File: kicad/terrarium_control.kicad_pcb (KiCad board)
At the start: 2 copper layers, 48 parts, among them J1 5V_IN, J10 220V_OUT, J11 LAMP0, J12 LAMP1, J13 I2C, J2 5V_OUT, J3 12V_IN, J4 SWITCHERS, J5 ICSP, J6 FUN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

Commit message: ~50% of board layout completed
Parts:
- added JP1: 0R, Resistor_SMD:R_1206_3216Metric_Pad1.30x1.75mm_HandSolder, F.Cu at (134.1, 64.1)
- BT1: footprint Battery:BatteryHolder_Keystone_106_1x20mm -> terrarium_control:batt_holder
- moved C3 158.4 mm to (125.9, 59.4), turned to 90 degrees
- moved C7 158.3 mm to (138.5, 59.9), turned to 180 degrees
- moved R5 125.8 mm to (149.1, 68.0), turned to 270 degrees
- moved BT1 123.4 mm to (146.4, 58.4)
- moved R10 122.0 mm to (137.8, 75.4), turned to 180 degrees
- moved R13 121.6 mm to (141.2, 75.4)
- moved U2 121.5 mm to (138.0, 79.9), turned to 270 degrees
- moved R9 120.6 mm to (121.3, 77.2), turned to 180 degrees
- moved C4 117.5 mm to (123.3, 59.8), turned to 90 degrees
- moved RN1 115.2 mm to (129.5, 74.5), turned to 270 degrees
- moved J3 97.8 mm to (142.0, 80.9), turned to 180 degrees
- moved R8 95.2 mm to (125.7, 77.2), turned to 180 degrees
- moved J13 91.3 mm to (138.0, 72.4), turned to 90 degrees
- moved J5 89.9 mm to (115.2, 67.7), turned to 180 degrees
- moved R6 89.0 mm to (133.3, 77.2), turned to 180 degrees
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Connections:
- net Net-(U3-Pad1) renamed /X+
- net Net-(U3-Pad2) renamed /X-
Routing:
- net SQW: track 0.00 -> 20.6 mm
- net +5V: track 14.4 -> 32.9 mm
- net SCL: track 6.27 -> 21.3 mm
- net GND: track 0.00 -> 14.8 mm
- net MCU_RXD: track 0.00 -> 13.3 mm
- net SDA: track 3.56 -> 15.7 mm
- net +BATT: track 0.00 -> 11.2 mm
- net MCU_TXD: track 0.00 -> 10.3 mm
- net DAC: track 0.00 -> 9.05 mm
- net Net-(R8-Pad2): track 0.00 -> 6.26 mm
- net DAC3: track 0.00 -> 5.57 mm
- net Net-(Q2-Pad1): track 0.00 -> 4.93 mm
- net FUN: track 0.00 -> 4.61 mm
- net Net-(R6-Pad2): track 0.00 -> 3.88 mm
- net Net-(R7-Pad2): track 0.00 -> 3.88 mm
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
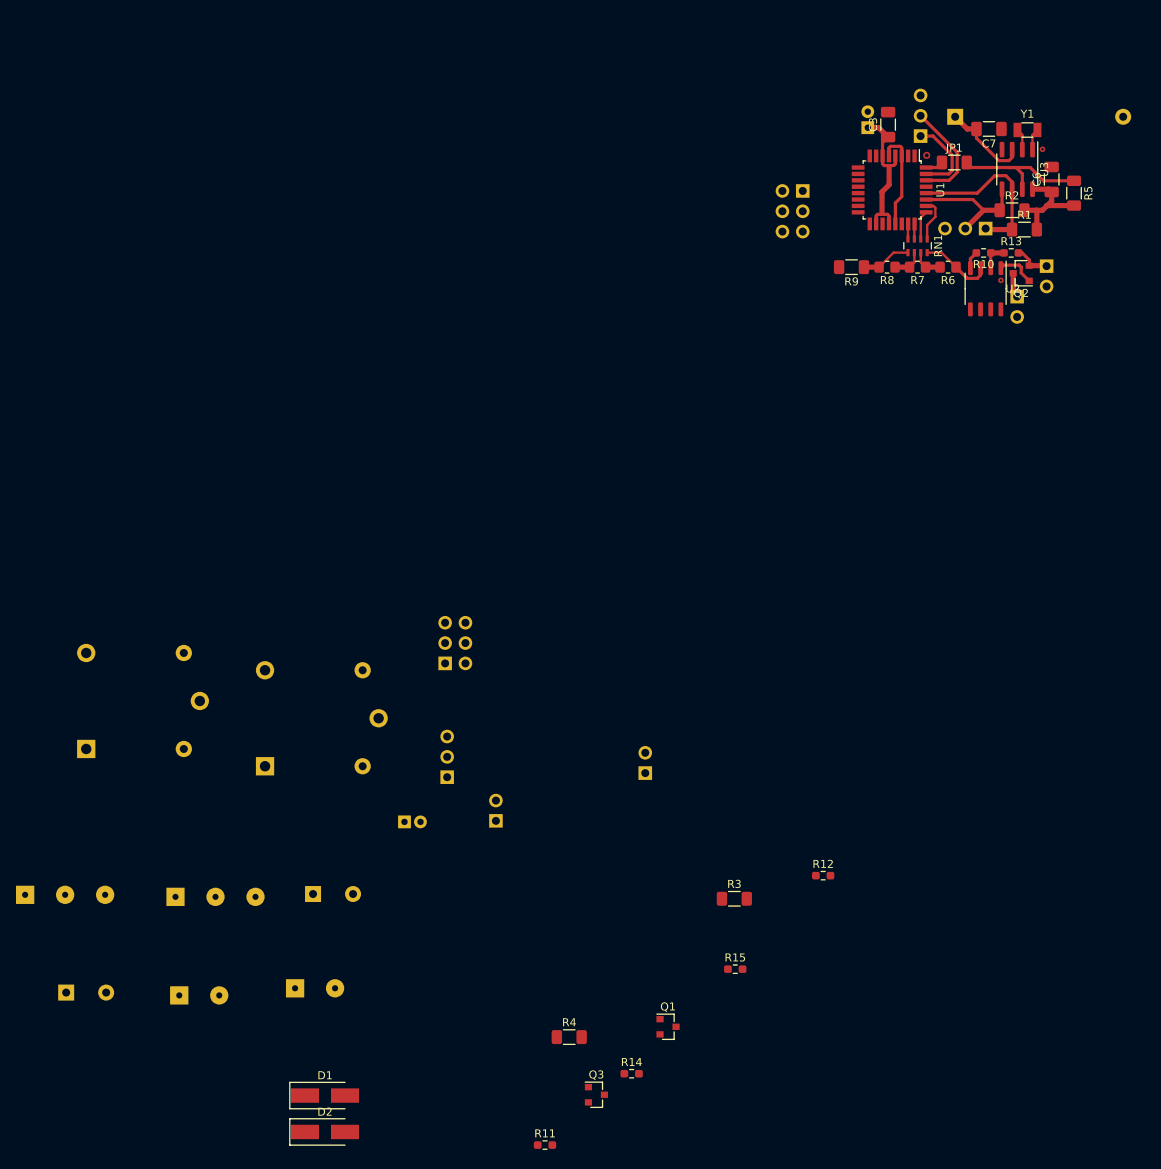
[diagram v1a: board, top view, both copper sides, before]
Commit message: Board layout completed
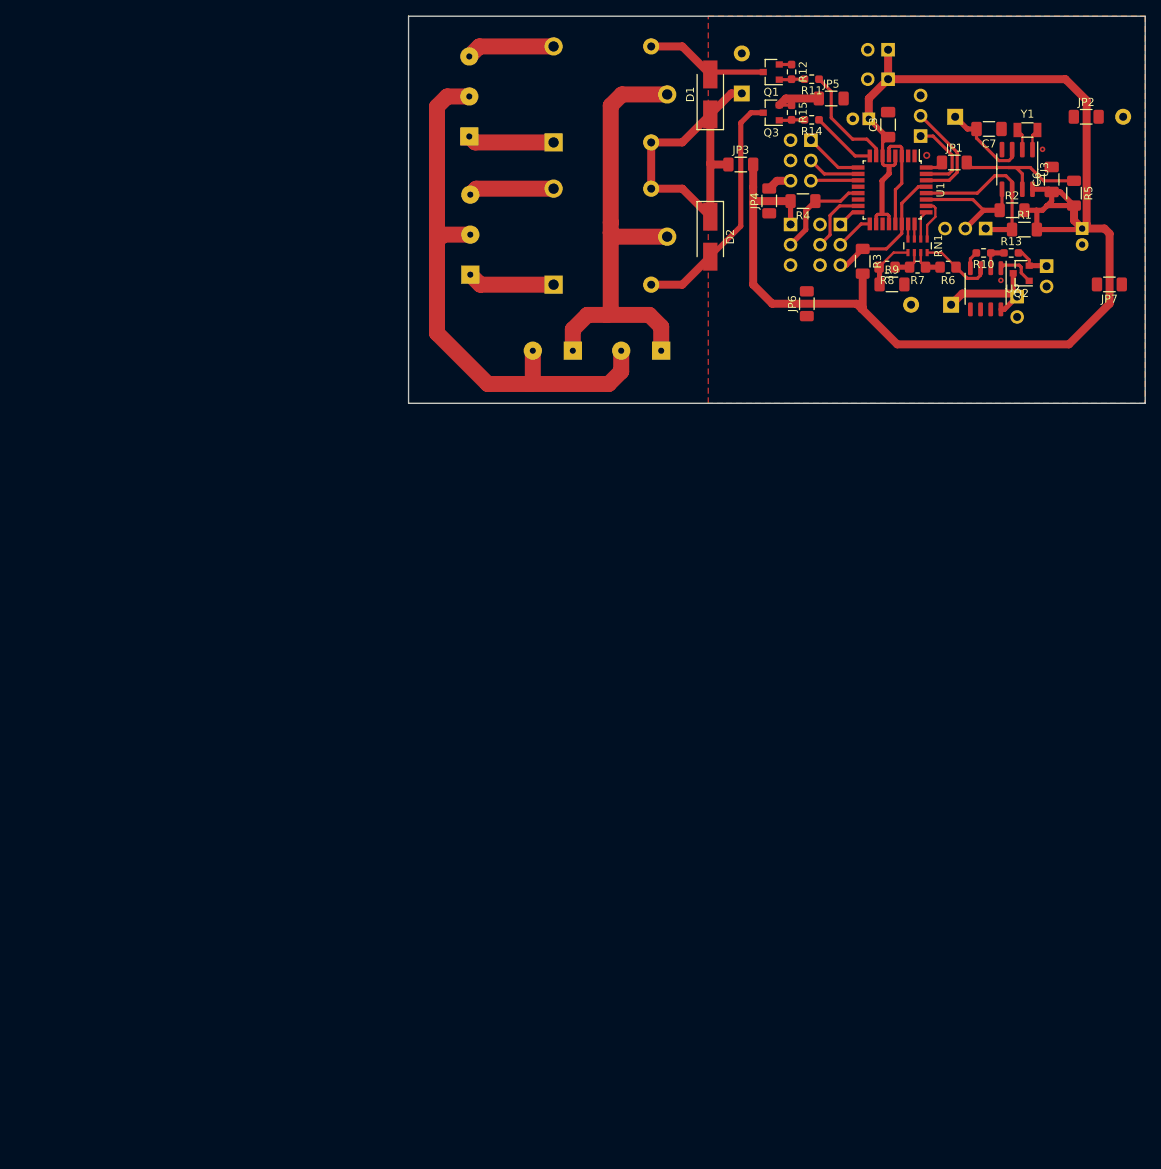
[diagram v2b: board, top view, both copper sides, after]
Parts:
- added JP2: 0R, Resistor_SMD:R_1206_3216Metric_Pad1.30x1.75mm_HandSolder, F.Cu at (150.6, 58.4)
- added JP3: 0R, Resistor_SMD:R_1206_3216Metric_Pad1.30x1.75mm_HandSolder, F.Cu at (107.4, 64.4)
- added JP4: 0R, Resistor_SMD:R_1206_3216Metric_Pad1.30x1.75mm_HandSolder, F.Cu at (111.0, 68.9)
- added JP5: 0R, Resistor_SMD:R_1206_3216Metric_Pad1.30x1.75mm_HandSolder, F.Cu at (118.7, 56.1)
- added JP6: 0R, Resistor_SMD:R_1206_3216Metric_Pad1.30x1.75mm_HandSolder, F.Cu at (115.7, 81.8)
- added JP7: 0R, Resistor_SMD:R_1206_3216Metric_Pad1.30x1.75mm_HandSolder, F.Cu at (153.5, 79.4)
- moved C1 140.6 mm to (107.6, 55.5), turned to 90 degrees
- moved R11 137.3 mm to (116.3, 53.7), turned to 180 degrees
- moved D1 134.1 mm to (103.6, 55.6), turned to 90 degrees
- moved Q3 124.7 mm to (111.3, 57.9), turned to 180 degrees
- moved D2 121.8 mm to (103.6, 73.4), turned to 270 degrees
- moved R14 121.3 mm to (116.3, 58.8), turned to 180 degrees
- moved Q1 120.0 mm to (111.3, 52.8), turned to 180 degrees
- moved C5 112.6 mm to (150.1, 72.4), turned to 270 degrees
- moved C2 108.6 mm to (133.7, 81.9), turned to 180 degrees
- moved R4 108.5 mm to (115.2, 69.0), turned to 180 degrees
- moved R15 107.3 mm to (113.8, 57.9), turned to 270 degrees
- moved J1 104.9 mm to (125.9, 53.7), turned to 90 degrees
- moved J11 104.8 mm to (73.4, 55.9), turned to 90 degrees
- moved R12 100.5 mm to (113.8, 52.8), turned to 270 degrees
- moved J12 96.7 mm to (73.5, 73.2), turned to 90 degrees
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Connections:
- J4 pad 2: FORCE0 -> GND
- J4 pad 3: FORCE1 -> FORCE0
- J4 pad 5: GND -> FORCE1
- K2 pad 3: Net-(D2-Pad2) -> +5V
- K2 pad 5: +5V -> Net-(D2-Pad2)
- U1 pad 22: Net-(U1-Pad22) -> RESET
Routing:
- net +5V: track 32.9 -> 230.5 mm
- net 220V_N: track 0.00 -> 70.6 mm
- net 220V_PHASE: track 0.00 -> 59.3 mm
- net Net-(D2-Pad2): track 0.00 -> 30.5 mm
- net RESET: track 0.00 -> 17.0 mm
- net Net-(D1-Pad2): track 0.00 -> 15.6 mm
- net RELAY0: track 0.00 -> 13.6 mm
- net ONE_WIRE: track 0.00 -> 12.5 mm
- net +12V: track 3.12 -> 14.9 mm
- net GND: track 14.8 -> 26.2 mm
- net Net-(J11-Pad3): track 0.00 -> 11.1 mm
- net Net-(J12-Pad1): track 0.00 -> 10.9 mm
- net Net-(J11-Pad1): track 0.00 -> 10.8 mm
- net Net-(J12-Pad3): track 0.00 -> 10.7 mm
- net RELAY1: track 0.00 -> 8.21 mm
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- added copper zone on F.Cu, net GND
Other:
- board outline added: 92.1 x 48.4 mm
- net class 220V: trace_width 1.5 -> 2

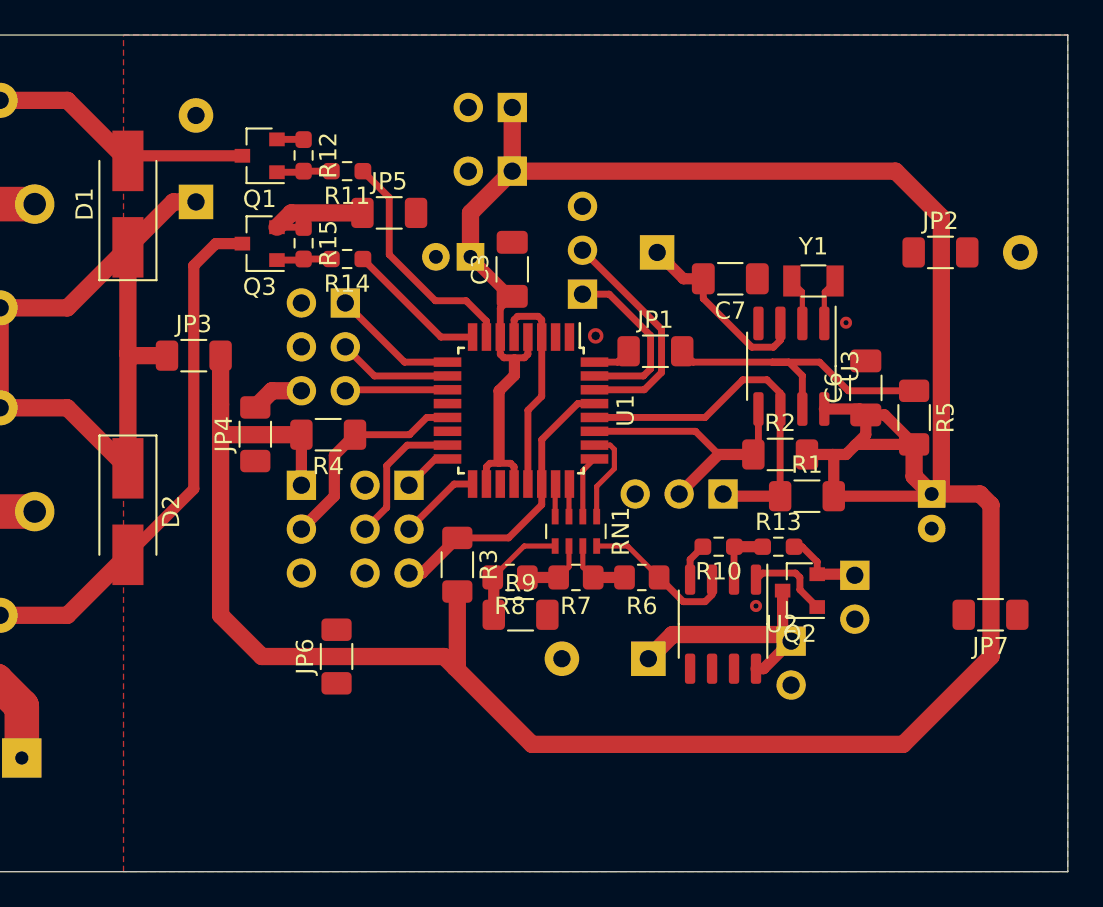
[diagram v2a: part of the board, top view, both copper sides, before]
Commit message: Add project name and github qrcode on pcb
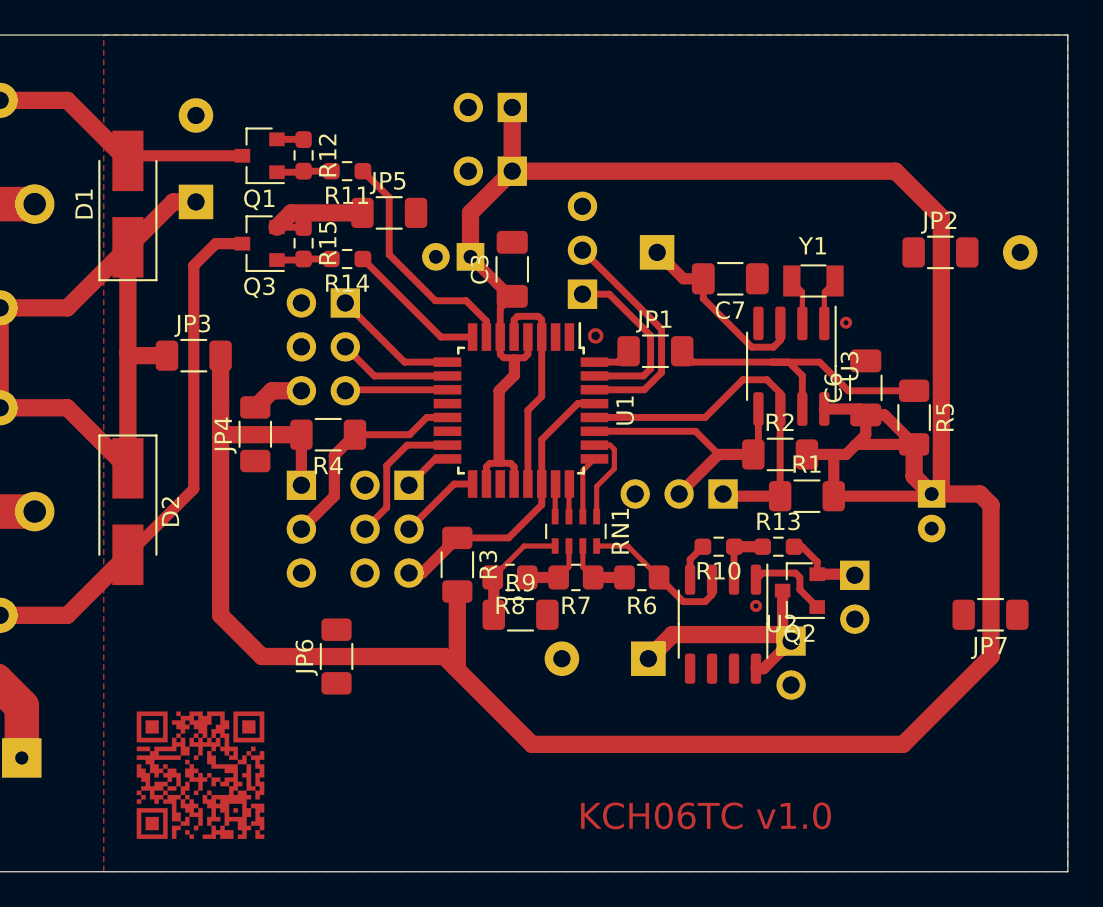
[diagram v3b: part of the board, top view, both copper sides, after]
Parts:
- added G***: LOGO, terrarium_control:github_qrcode, F.Cu at (107.8, 88.6)
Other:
- board text added: "KCH06TC v1.0"

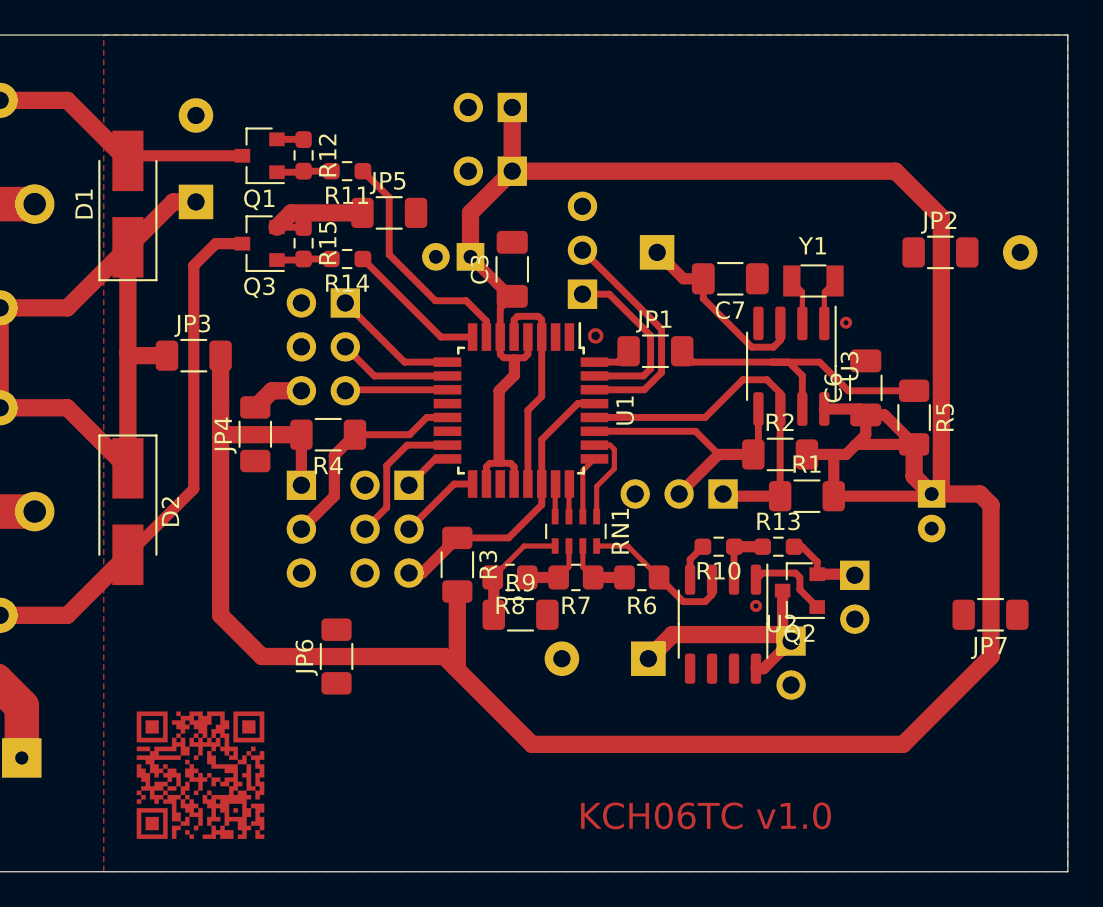
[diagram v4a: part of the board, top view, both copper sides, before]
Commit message: Work on bugs: Remove QR-code; Change track distance to 0.24 mm; Add plain ground tracks instead of filler zone.
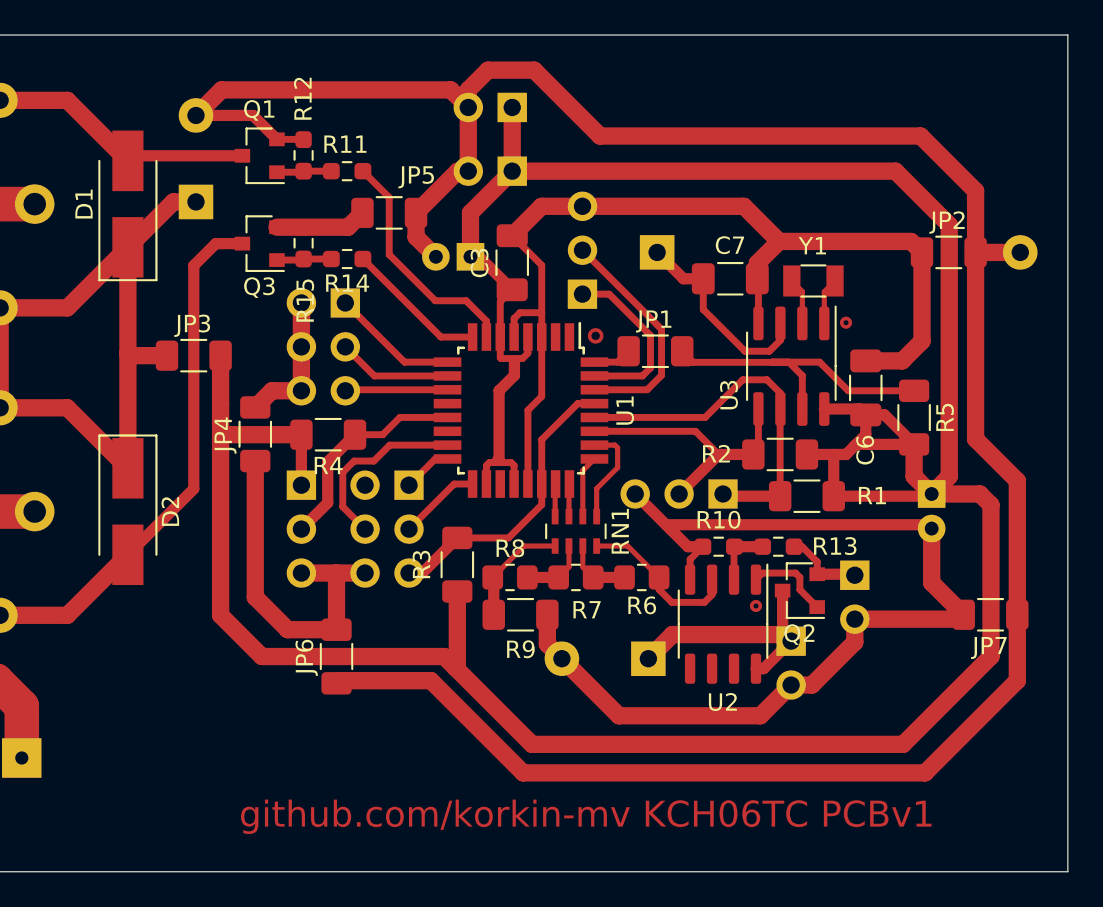
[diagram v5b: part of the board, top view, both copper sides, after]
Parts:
- removed G***: LOGO, terrarium_control:github_qrcode
- moved JP2 0.48 mm to (151.1, 58.4)
- moved C3 0.38 mm to (125.9, 59.0)
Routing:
- net GND: track 26.2 -> 294.7 mm
- net MOSI: track 8.20 -> 10.5 mm
- net +5V: track 230.5 -> 231.4 mm
- net +BATT: track 11.2 -> 11.8 mm
- removed copper zone on F.Cu, net GND
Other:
- net class Default: clearance 0.2 -> 0.24
- rule trace_clearance: 0.2 -> 0.24
- board text added: "github.com/korkin-mv KCH06TC PCBv1"
- board text removed: "KCH06TC v1.0"

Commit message: Board changed from single-sided to double-sided.
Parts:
- removed JP1, JP2, JP3, JP4, JP5, JP6, JP7: 0R, Resistor_SMD:R_1206_3216Metric_Pad1.30x1.75mm_HandSolder
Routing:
- net GND: track 294.7 -> 15.0 mm
- net +5V: track 231.4 -> 187.8 mm, vias 0 -> 1
- net MCU_RXD: track 13.4 -> 15.8 mm
- net MCU_TXD: track 10.2 -> 11.8 mm
- net RELAY0: track 13.6 -> 14.6 mm, vias 0 -> 2
- net SQW: track 20.6 -> 21.6 mm, vias 0 -> 2
- added copper zone on B.Cu, net GND
- added copper zone on F.Cu, net GND
